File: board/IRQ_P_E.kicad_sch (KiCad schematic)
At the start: 18 parts, among them IC5 74LS219, IC6 74LS219, IC7 74LS219, IC8 74LS219, U42 74F157, U43 74F157, U44 74LS148, U45 74LS148, U46 74F32

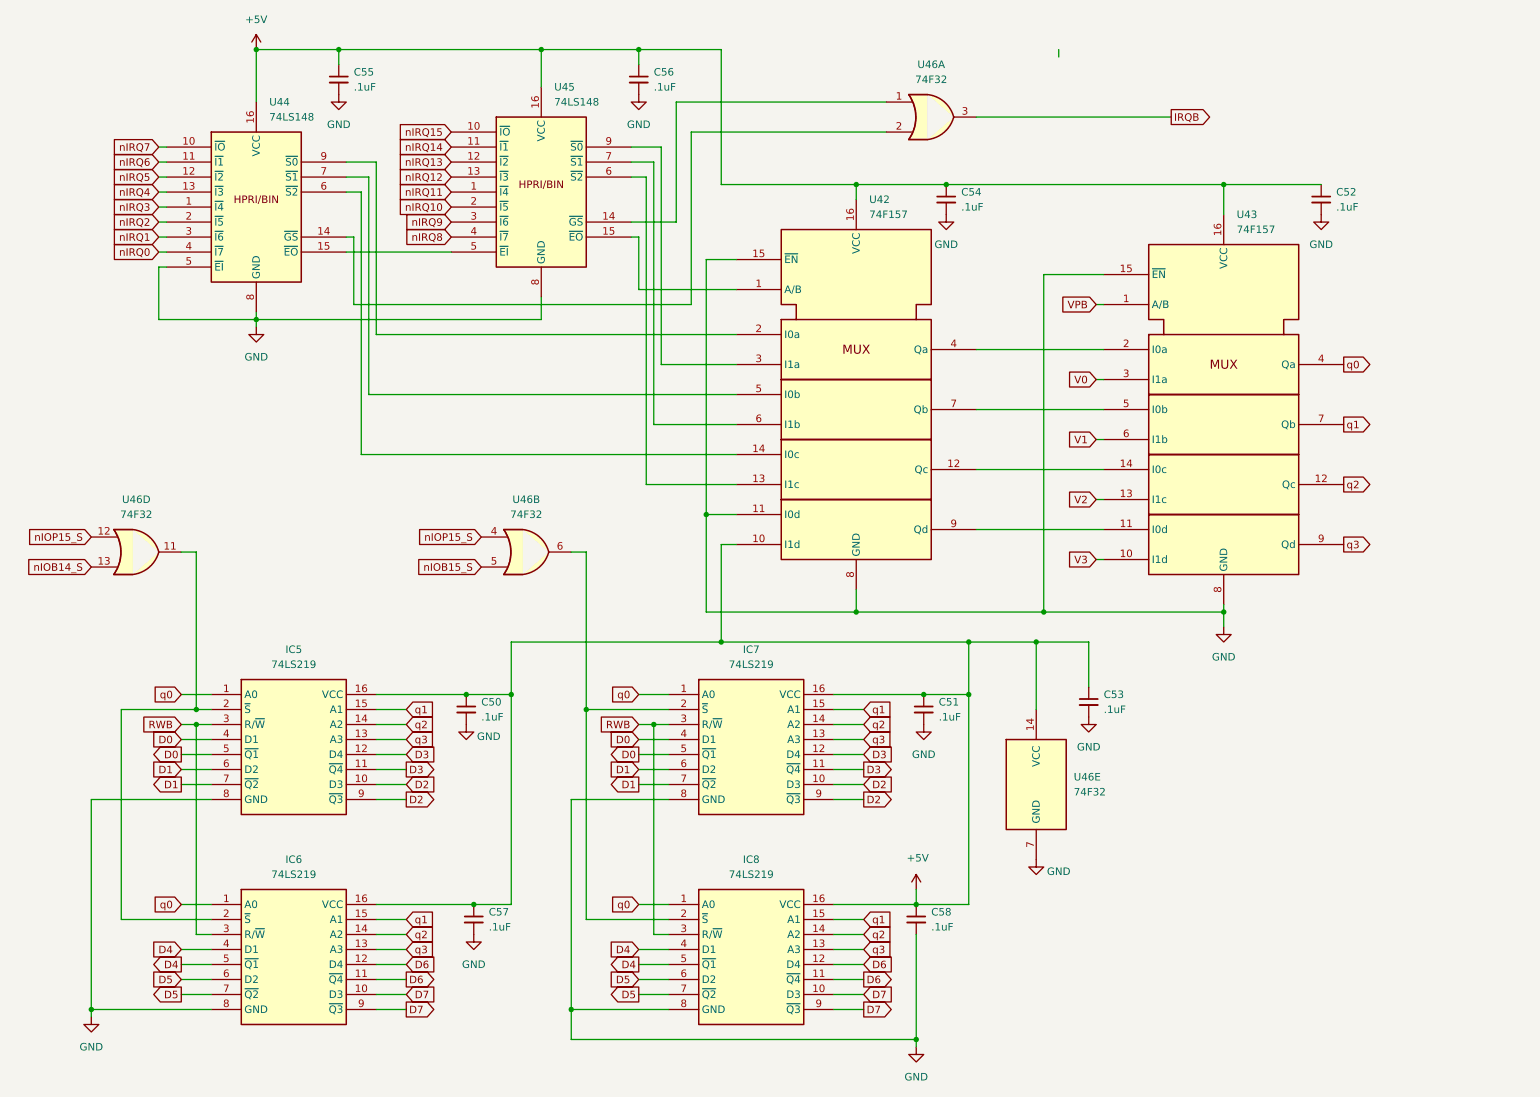
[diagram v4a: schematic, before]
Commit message: Schematic Bus updates, silkscreen updates, position tweaks, and other corrections.
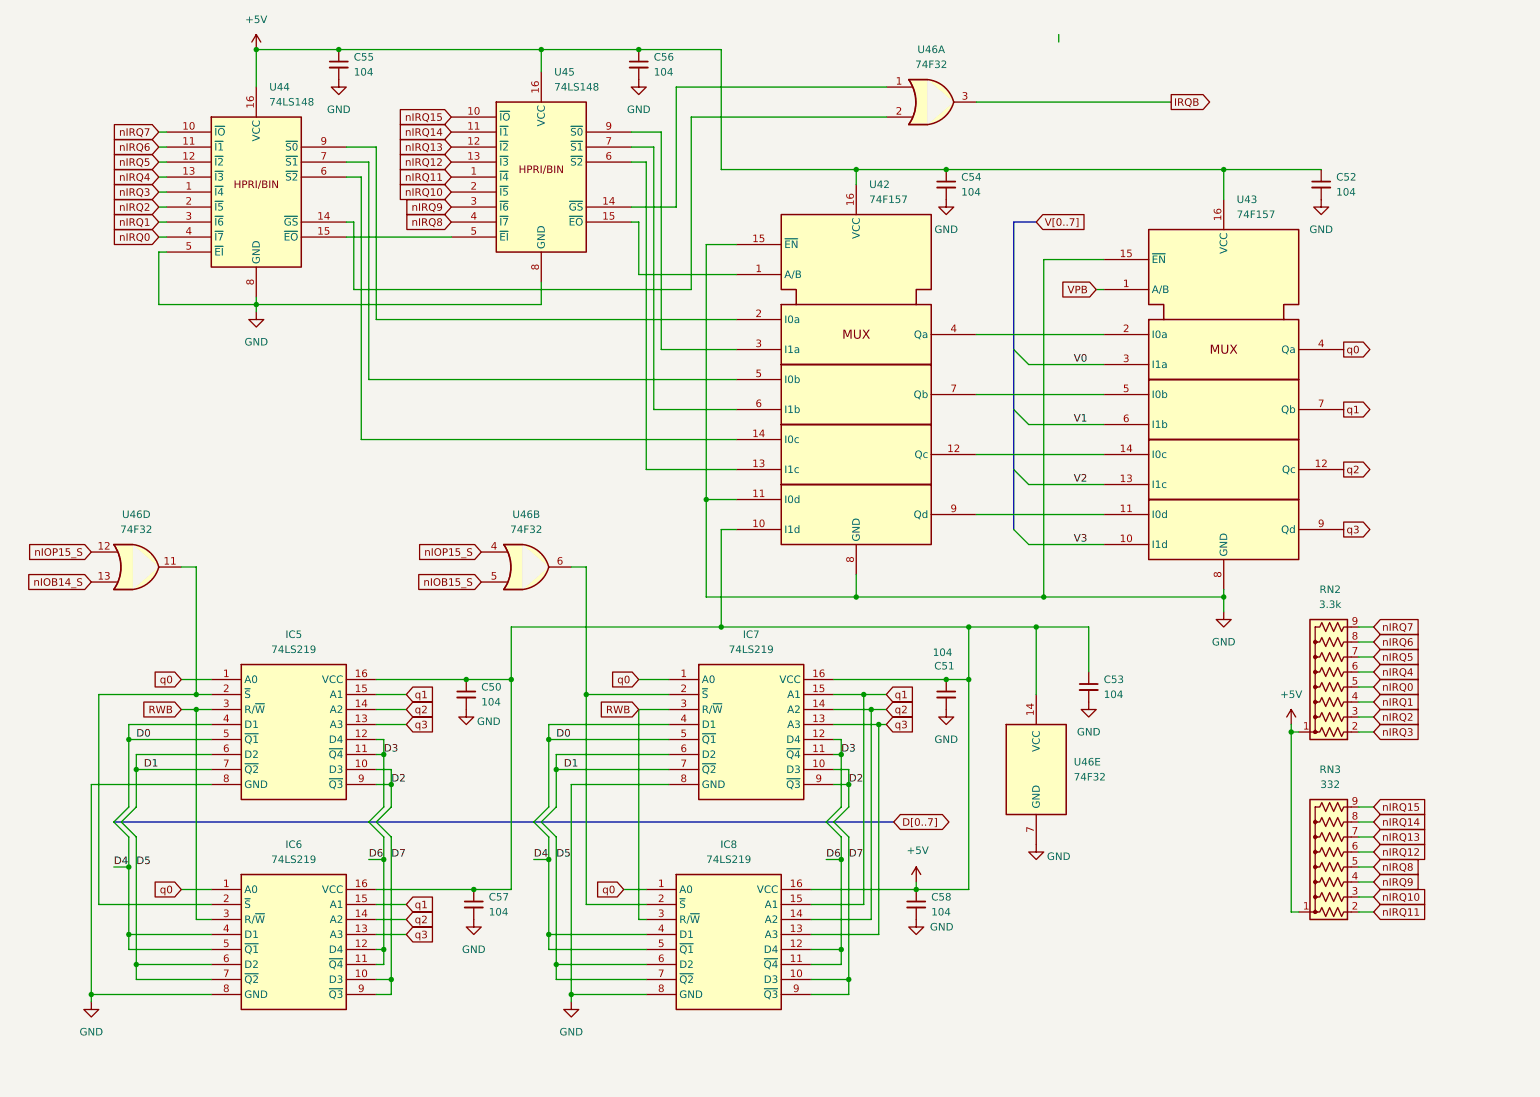
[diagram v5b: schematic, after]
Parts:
- added RN2: 3.3k, Resistor_THT:R_Array_SIP9, symbol Device:R_Network08_US
- added RN3: 332, Resistor_THT:R_Array_SIP9, symbol Device:R_Network08_US
- C50, C51, C52, C53, C54, C55, C56, C57, C58: value .1uF -> 104
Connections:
- net +5V: now also RN2.1 (common), RN3.1 (common)
- net nIRQ0: now also RN2.5 (R4)
- net nIRQ1: now also RN2.4 (R3)
- net nIRQ10: now also RN3.3 (R2)
- net nIRQ11: now also RN3.2 (R1)
- net nIRQ12: now also RN3.6 (R5)
- net nIRQ13: now also RN3.7 (R6)
- net nIRQ14: now also RN3.8 (R7)
- net nIRQ15: now also RN3.9 (R8)
- net nIRQ2: now also RN2.3 (R2)
- net nIRQ3: now also RN2.2 (R1)
- net nIRQ4: now also RN2.6 (R5)
- net nIRQ5: now also RN2.7 (R6)
- net nIRQ6: now also RN2.8 (R7)
- net nIRQ7: now also RN2.9 (R8)
- net nIRQ8: now also RN3.5 (R4)
- net nIRQ9: now also RN3.4 (R3)
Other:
- company: (none) -> Data Tuning
- title: (none) -> IRQ Priority Logic and Vector Memory
- moved on the sheet: C50, C51, C52, C53, C54, C55, C56, C57, C58, IC5, IC6, IC7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

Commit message: More PCB position tweaks.
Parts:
- RN2: value 3.3k -> 332
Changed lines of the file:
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@@
 			)
 		)
-		(property "Value" "3.3k"
+		(property "Value" "332"
 			(at 236.474 114.3 90)
 			(effects

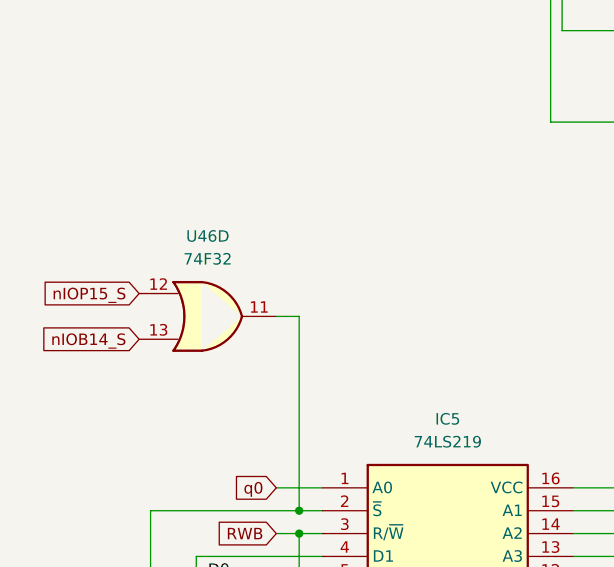
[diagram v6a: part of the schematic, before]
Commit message: Added VIA port A header and voltage protection diode package socket. Updated logic.
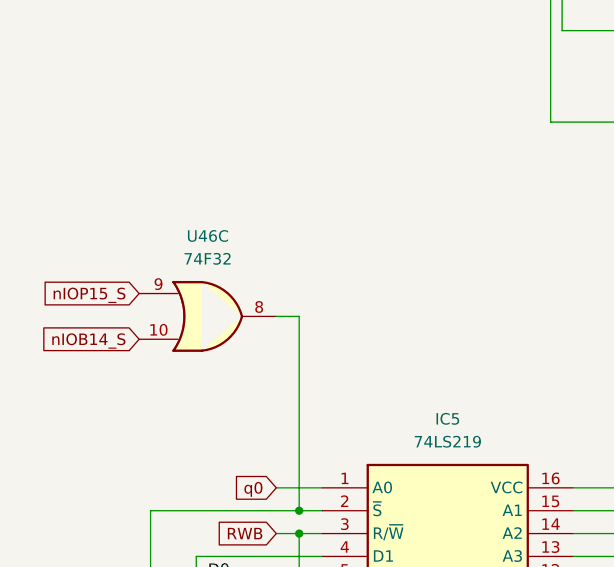
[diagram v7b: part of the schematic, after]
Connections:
- net nIOB14_S: now also U46.10; no longer U46.13
- net nIOP15_S: now also U46.9; no longer U46.12
- net at IC5.2 (~{S}), IC6.2 (~{S}): now also U46.8; no longer U46.11
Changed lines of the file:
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@@
 		(lib_id "74xx:74LS32")
 		(at 34.29 107.95 0)
-		(unit 4)
+		(unit 3)
 		(exclude_from_sim no)
 		(in_bom yes)
@@
 				(path "/ef29fc71-3fec-48b5-8a1a-46bee537a98c/9e82ed5b-af5c-4fee-b6ce-87e97255963b/1bce60c3-d882-492e-9aec-170cf0780040"
 					(reference "U46")
-					(unit 4)
+					(unit 3)
 				)
 			)
